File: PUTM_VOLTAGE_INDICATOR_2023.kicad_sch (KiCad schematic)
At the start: 15 parts, among them IC1 LM211DT, J1 HV+, J2 HV-

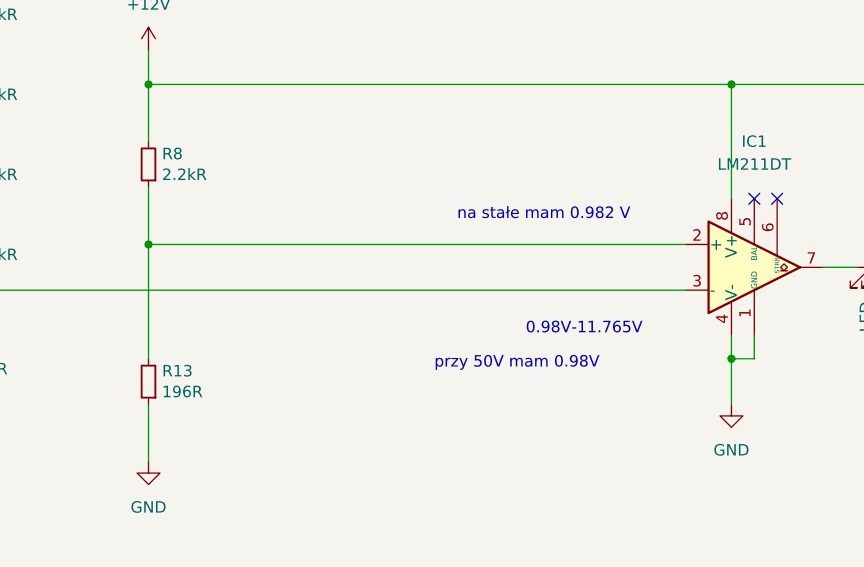
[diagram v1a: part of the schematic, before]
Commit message: symbol changed / resistor values changed
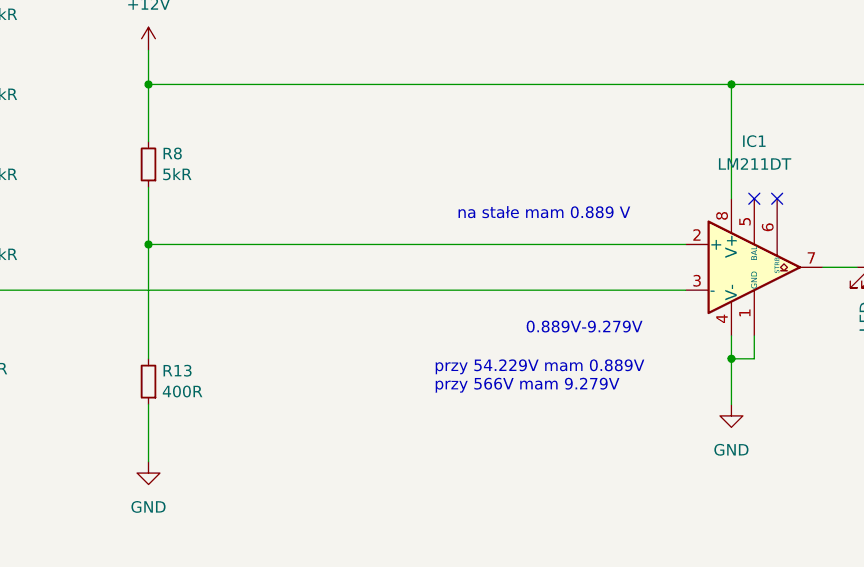
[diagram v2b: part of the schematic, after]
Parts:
- R13: value 196R -> 400R
- R8: value 2.2kR -> 5kR
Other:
- note added: "0.889V-9.279V"
- note added: "na stałe mam 0.889 V"
- note added: "przy 54.229V mam 0.889V przy 566V mam 9.279V"
- note removed: "0.98V-11.765V"
- note removed: "na stałe mam 0.982 V"
- note removed: "przy 50V mam 0.98V"
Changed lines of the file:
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@@
     (effects (font (size 1.27 1.27)) (justify left bottom))
   )
-  (text "przy 50V mam 0.98V" (at 111.76 113.03 0)
+  (text "przy 54.229V mam 0.889V\nprzy 566V mam 9.279V" (at 111.76 115.57 0)
     (effects (font (size 1.27 1.27)) (justify left bottom))
   )
-  (text "na stałe mam 0.982 V\n" (at 114.3 96.52 0)
+  (text "na stałe mam 0.889 V\n" (at 114.3 96.52 0)
     (effects (font (size 1.27 1.27)) (justify left bottom))
   )
-  (text "0.98V-11.765V\n" (at 121.92 109.22 0)
+  (text "0.889V-9.279V\n" (at 121.92 109.22 0)
     (effects (font (size 1.27 1.27)) (justify left bottom))
   )
@@
       (effects (font (size 1.27 1.27)) (justify right))
     )
-    (property "Value" "196R" (id 1) (at 81.5086 115.443 0)
+    (property "Value" "400R" (id 1) (at 81.5086 115.443 0)
       (effects (font (size 1.27 1.27)) (justify right))
     )
@@
       (effects (font (size 1.27 1.27)) (justify right))
     )
-    (property "Value" "2.2kR" (id 1) (at 81.5086 91.313 0)
+    (property "Value" "5kR" (id 1) (at 81.5086 91.313 0)
       (effects (font (size 1.27 1.27)) (justify right))
     )
@@
     )
     (path "/506a5e4b-56b3-48e0-a817-85ff29fd97cd"
-      (reference "R8") (unit 1) (value "2.2kR") (footprint "Resistor_SMD:R_0603_1608Metric")
+      (reference "R8") (unit 1) (value "5kR") (footprint "Resistor_SMD:R_0603_1608Metric")
     )
     (path "/43073a32-87a0-40f0-a31c-d6ff06a9a96e"
-      (reference "R13") (unit 1) (value "196R") (footprint "Resistor_SMD:R_0603_1608Metric")
+      (reference "R13") (unit 1) (value "400R") (footprint "Resistor_SMD:R_0603_1608Metric")
     )
     (path "/8f056ae7-3800-4073-a3d5-68da1f6309ab"

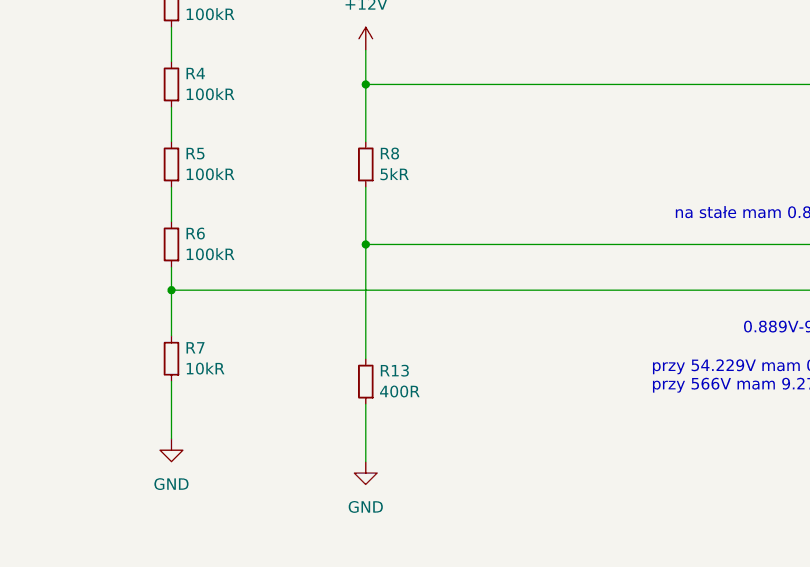
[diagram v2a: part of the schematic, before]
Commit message: pcb update / resistor values
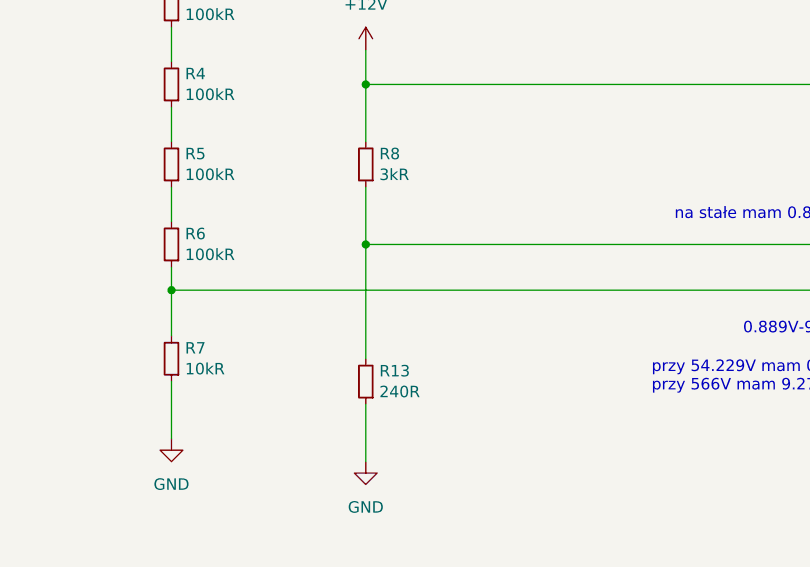
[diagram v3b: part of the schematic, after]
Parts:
- R13: value 400R -> 240R
- R8: value 5kR -> 3kR
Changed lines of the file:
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@@
       (effects (font (size 1.27 1.27)) (justify right))
     )
-    (property "Value" "400R" (id 1) (at 81.5086 115.443 0)
+    (property "Value" "240R" (id 1) (at 81.5086 115.443 0)
       (effects (font (size 1.27 1.27)) (justify right))
     )
@@
       (effects (font (size 1.27 1.27)) (justify right))
     )
-    (property "Value" "5kR" (id 1) (at 81.5086 91.313 0)
+    (property "Value" "3kR" (id 1) (at 81.5086 91.313 0)
       (effects (font (size 1.27 1.27)) (justify right))
     )
@@
     )
     (path "/506a5e4b-56b3-48e0-a817-85ff29fd97cd"
-      (reference "R8") (unit 1) (value "5kR") (footprint "Resistor_SMD:R_0603_1608Metric")
+      (reference "R8") (unit 1) (value "3kR") (footprint "Resistor_SMD:R_0603_1608Metric")
     )
     (path "/43073a32-87a0-40f0-a31c-d6ff06a9a96e"
-      (reference "R13") (unit 1) (value "400R") (footprint "Resistor_SMD:R_0603_1608Metric")
+      (reference "R13") (unit 1) (value "240R") (footprint "Resistor_SMD:R_0603_1608Metric")
     )
     (path "/8f056ae7-3800-4073-a3d5-68da1f6309ab"
